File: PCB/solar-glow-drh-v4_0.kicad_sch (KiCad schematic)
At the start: 68 parts, among them J1 UPDI hdr, Q2 DMG1012T, SW2 LED master, U1 AVR64EA28 (VQFN28), U3 ADXL367, U5 NT3H2211, U6 TPS22916C, U7 MB85RC512TY, U8 AEM10300, U9 TPS7A0233PDQNR

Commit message: U6 goes on the board as the DSBGA -- the swap round closes: 0 parity, 0 unconnected, exact ledger, suite 20/20
The board half of the 2026-08-06 ultrathin round, on DRH's rework upload
(merged from main; his Q2 SOT-523 and C9 0603 lands and all wiring kept
verbatim, his sch upload superseded by the branch's -- verified semantically
identical minus the TC1 debug nets).

U6: SC-70 out, solarglow:TPS22916_YFP0004 in at the same centroid, B.Cu,
rot 180 -- chosen so ON's ball sits on R14's x (straight shot north to the
existing junction), VIN diagonals SE to C4.1, VOUT takes one via down and
runs F.Cu east into the old VNFC via's position (that via and its teardrops
retired -- one via total, net fewer than before), GND spokes from the pour.
C6's VS branch rejoins the trunk at its top corner, retiring the dead pad
junction. Ball nets bound A2=VS A1=VNFC B1=GND B2=NFC_EN; fields stamped
from the schematic; silk ref raised to the board's 0.8 floor. NO teardrops
on the balls BY DESIGN -- 0.17 air gap vs the 0.152 floor (README).

TC1: DRH's pad-net choice wins -- sch labels swapped to match his copper
(5=SCL, 6=SDA; 4=BTN stands). His 15 'fix this' exclusions all died with
the swap and the net binding; purged, the 14 ledgered ones kept.

Flow-down: heights U6 1.10->0.50, Q2 1.20->0.90, C9 1.25->0.90 (Diodes
SOT523 A1+A2 max verified from the in-repo sheet); PENDING_FOOTPRINT_SYNC
emptied (all three synced -- stale entries are errors by design); Q2 gets
DIODES_SOT523.step, the missing-stock-model class's third arrival after
U7/U9 (KiCad's SOT-523 footprint names a model kicad-packages3D never
shipped); mask art re-applied (front changed: the VNFC F.Cu run + DRH's
TC1 routing) and MATCHing; coil check OK at C9 47 pF.

Glow window re-measured, teardrop-inclusive, in-aperture: D2 0.3740,
D3 1.2033, D4 1.8112, D5 0.7580 -- bit-identical to the 2026-08-05
baseline. New standing number: INT1-INT2 cross the window at exactly
0.1520 (floor-exact, mid-track, no pads -- not the no-mask-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
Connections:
- net SCL: now also TC1.5, TC1/b1.5; no longer TC1.6, TC1/b1.6
- net SDA: now also TC1.6, TC1/b1.6; no longer TC1.5, TC1/b1.5
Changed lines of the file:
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@@
 		)
 	)
-	(global_label "SDA"
+	(global_label "SCL"
 		(shape bidirectional)
 		(at 405.13 139.7 0)
@@
 		)
 	)
-	(global_label "SCL"
+	(global_label "SDA"
 		(shape bidirectional)
 		(at 405.13 144.78 0)
@@
 		)
 	)
-	(global_label "SDA"
+	(global_label "SCL"
 		(shape bidirectional)
 		(at 405.13 171.45 0)
@@
 		)
 	)
-	(global_label "SCL"
+	(global_label "SDA"
 		(shape bidirectional)
 		(at 405.13 176.53 0)

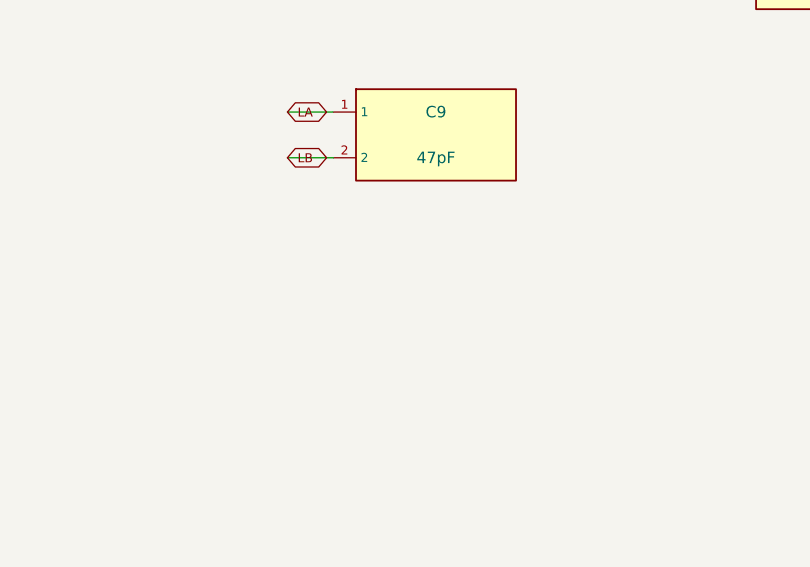
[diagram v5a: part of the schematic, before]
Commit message: C30 -- a DNP trim pad in parallel with C9, the tank's granular-refinement knob
DRH approved the extra pad; here it is, both sides of the parity line.
Schematic: solarglow:C30 (cloned lib symbol), instance at C9's column
wired LA/LB through the same global-label idiom, in_bom no / dnp yes /
in_pos_files no. Board: 0402 at (34.35, 37.95) rot 90, 1.36 mm west of
C9, pads stubbed 0.3 mm-wide to C9's own pads (the tank's track width),
attr smd + exclude_from_pos_files + exclude_from_bom + dnp. NO 3D model
BY CHOICE: the dnp-with-a-model render blind spot (the C9-of-old class)
stays an empty class, and CLAUDE.md's dnp recount moves 12 -> 13 with
the reason.

Why it earns its pads: bench granularity finer than swapping C9
outright, and the AIR variant's retune has a home -- the open 316L
frame drops the ferrite, L falls toward the bare 0.958 uH, f0 rises,
and the correction is MORE parallel C: exactly the direction a parallel
pad adds. (C9's own history ran the other way: the 82 pF + DNP
arrangement of the pre-2026-07-30 tune sat UNDER the carrier. This pad
cannot repeat that mistake -- C9's 47 pF keeps the enclosed tank above
13.56 on its own, and C30 only ever pulls DOWN toward it.)

Verified: ERC 3 pre-existing excluded warnings only (grid-snapped after
the first pass caught my off-grid 15.62 offset -- 16.51 is 13 steps);
parity DRC NO unexcluded errors, 0 unconnected (one courtyard kiss
found and fixed by the 0.25 westward shift); mask_art MATCH;
consistency 0/0. Buy documents untouched by construction: dnp keeps C30
out of the BOM, the CPL, and check [15]'s ledger until a value exists.

Co-Authored-By: Claude Fable 5 <noreply@anthropic.com>
Claude-Session: https://claude.ai/code/session_015D4iTho3BuNxSQyJmyaxvg
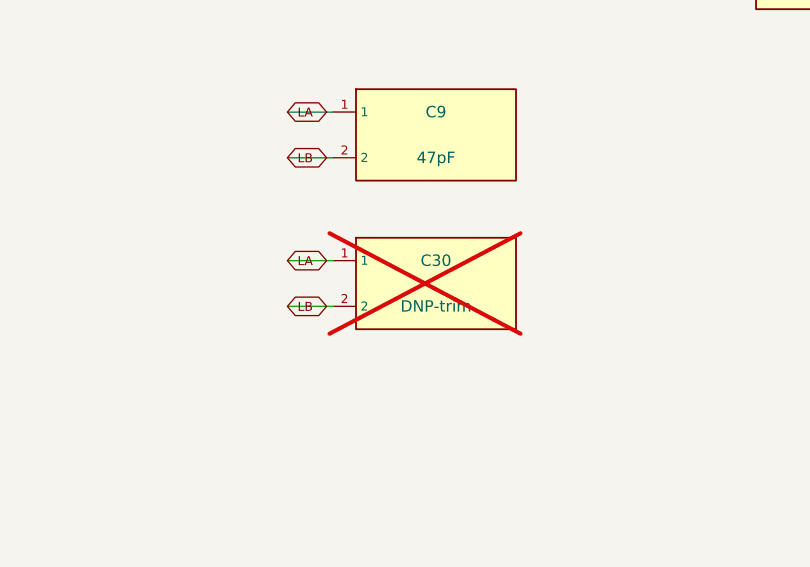
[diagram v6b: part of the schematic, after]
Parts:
- added C30: DNP-trim, Capacitor_SMD:C_0402_1005Metric, symbol solarglow:C30
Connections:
- net LA: now also C30.1
- net LB: now also C30.2
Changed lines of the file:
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@@
 	)
 	(symbol
+		(lib_id "solarglow:C30")
+		(at 560.07 135.89 0)
+		(unit 1)
+		(body_style 1)
+		(exclude_from_sim no)
+		(in_bom no)
+		(on_board yes)
+		(in_pos_files no)
+		(dnp yes)
+		(property "Reference" "C30"
+			(at 571.5 135.89 0)
+			(show_name no)
+			(do_not_autoplace no)
+			(effects
+				(font
+					(size 1.27 1.27)
+				)
+			)
+		)
+		(property "Value" "DNP-trim"
+			(at 571.5 140.97 0)
+			(show_name no)
+			(do_not_autoplace no)
+			(effects
+				(font
+					(size 1.27 1.27)
+				)
+			)
+		)
+		(property "Footprint" "Capacitor_SMD:C_0402_1005Metric"
+			(at 571.5 129.54 0)
+			(hide yes)
+			(show_name no)
+			(do_not_autoplace no)
+			(effects
+				(font
+					(size 1.27 1.27)
+				)
+			)
+		)
+		(property "Datasheet" ""
+			(at 560.07 135.89 0)
+			(hide yes)
+			(show_name no)
+			(do_not_autoplace no)
+			(effects
+				(font
+					(size 1.27 1.27)
+				)
+			)
+		)
+		(property "Description" "C9 tank trim pad, DNP (2026-08-07). Parallel with C9 across LA/LB: bench granularity for the paper-tune ladder, and headroom for the AIR variant retune -- the open 316L frame drops the ferrite, L falls toward the bare 0.958 uH, f0 rises, and the fix is MORE C in parallel: exactly what this pad adds. Fit a High-Q C0G 0402 chosen at the bench; stays out of every buy document until a value exists (dnp + exclude_from_bom + exclude_from_pos_files)."
+			(at 560.07 135.89 0)
+			(hide yes)
+			(show_name no)
+			(do_not_autoplace no)
+			(effects
+				(font
+					(size 1.27 1.27)
+				)
+			)
+		)
+		(property "MPN" "QSCP251Q470G1GV001T"
+			(at 560.07 135.89 0)
+			(hide yes)
+			(show_name no)
+			(do_not_autoplace no)
+			(effects
+				(font
+					(size 1.27 1.27)
+				)
+			)
+		)
+		(property "Manufacturer" "Johanson Technology"
+			(at 560.07 135.89 0)
+			(hide yes)
+			(show_name no)
+			(do_not_autoplace no)
+			(effects
+				(font
+					(size 1.27 1.27)
+				)
+			)
+		)
+		(property "Supplier" "DigiKey"
+			(at 560.07 135.89 0)
+			(hide yes)
+			(show_name no)
+			(do_not_autoplace no)
+			(effects
+				(font
+					(size 1.27 1.27)
+				)
+			)
+		)
+		(property "Supplier P/N" "712-QSCP251Q470G1GV001TCT-ND"
+			(at 560.07 135.89 0)
+			(hide yes)
+			(show_name no)
+			(do_not_autoplace no)
+			(effects
+				(font
+					(size 1.27 1.27)
+				)
+			)
+		)
+		(pin "1"
+		)
+		(pin "2"
+		)
+		(instances
+			(project "solar-glow-drh-v4_0"
+				(path "/bf17630f-b49b-49a7-9335-83fa0a7a44d0"
+					(reference "C30")
+					(unit 1)
+				)
+			)
+		)
+	)
+	(symbol
 		(lib_id "solarglow:SC1")
 		(at 80.01 38.1 0)
@@
 		)
 	)
+	(global_label "LA"
+		(shape bidirectional)
+		(at 554.99 135.89 0)
+		(effects
+			(font
+				(size 1 1)
+			)
+		)
+		(property "Intersheetrefs" "${INTERSHEET_REFS}"
+			(at 554.99 135.89 0)
+			(hide yes)
+			(show_name no)
+			(do_not_autoplace no)
+			(effects
+				(font
+					(size 1.27 1.27)
+				)
+			)
+		)
+	)
+	(global_label "LB"
+		(shape bidirectional)
+		(at 554.99 140.97 0)
+		(effects
+			(font
+				(size 1 1)
+			)
+		)
+		(property "Intersheetrefs" "${INTERSHEET_REFS}"
+			(at 554.99 140.97 0)
+			(hide yes)
+			(show_name no)
+			(do_not_autoplace no)
+			(effects
+				(font
+					(size 1.27 1.27)
+				)
+			)
+		)
+	)
+	(wire
+		(pts
+			(xy 560.07 135.89) (xy 554.99 135.89)
+		)
+		(stroke
+			(width 0)
+			(type default)
+		)
+	)
+	(wire
+		(pts
+			(xy 560.07 140.97) (xy 554.99 140.97)
+		)
+		(stroke
+			(width 0)
+			(type default)
+		)
+	)

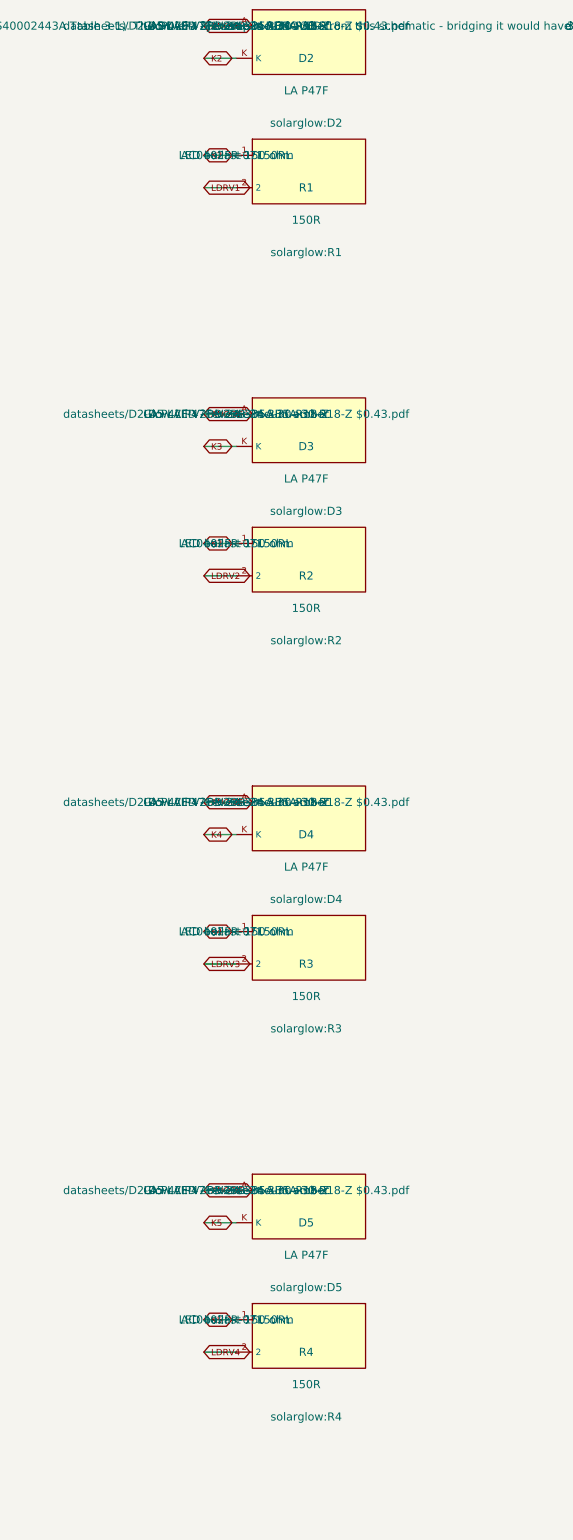
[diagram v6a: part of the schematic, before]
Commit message: RN1 -- DRH's 4-in-1 ballast array, identified, verified, and flowed through the whole repo
DRH drew the copper (KiCad R_Array_Convex_4x0402 land, mid-board at
(32.03, 49.84), R1-R4 deleted); this finishes everything downstream.

THE PART, from a 12-agent verified sourcing sweep (3 finders, 8
adversarial verifies, 1 judge; every claim pulled from the live catalog
or DigiKey page): Panasonic EXB-28V151JX, 4x150R isolated, 0804 convex.
The +/-1% grades all failed procurement reality (Yageo YC124-FR is
marketplace-only at 10k MOQ/17wk; KOA CN1E4 family-EOL; CTS unlisted),
making J +/-5% the buyable ceiling -- the tie broke on AEC-Q200 Grade 1
in the CURRENT catalog (Yageo WITHDREW their claim in DS V.11 Sep 2025;
DigiKey's attribute is stale against it), 0.45 max height (0.15 under
the lite brace's 0.60 span), 136,179 live DigiKey stock, and the
strongest pairing evidence in the pool: the catalog PRINTS the pin
numbers -- elements 1-8/2-7/3-6/4-5, IC-style -- matching the board's
wiring exactly. A different convention would PERMUTE the LED channels;
that check was load-bearing, not paranoia. Sourcing record lives in
RN1's own Description field. Runner-up: YC124-JR-07150RL.

Schematic: R1-R4 excised whole (instances, lib defs, wires, labels);
solarglow:RN1 8-pin symbol wired through the same global-label idiom,
pin-for-pin to the board (parity proves it: 0 unconnected, 0 field
mismatches). Board: footprint annotated RN1, linked to the schematic
uuid, MPN/Manufacturer/Supplier P/N mirrored. The stock land's own
0.150 inter-pad gap (2um under the 0.152 floor) fixed BY DESIGN: inner
pads slimmed 0.300 -> 0.294 -> gap 0.153, no exclusions carried;
PCB/README's re-link warning box records it so Update-Footprints-from-
Library cannot silently revert it.

Flow-down: part_heights RN1 0.45 (catalog T max); check [20]'s
OPAQUE_PN_LEDGER gains ("EXB-28V151JX","Y7151CT-ND") and drops the
orphaned R1-R4 Yageo pair per its own instruction (with a syntax
mishap en route: a naive insert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
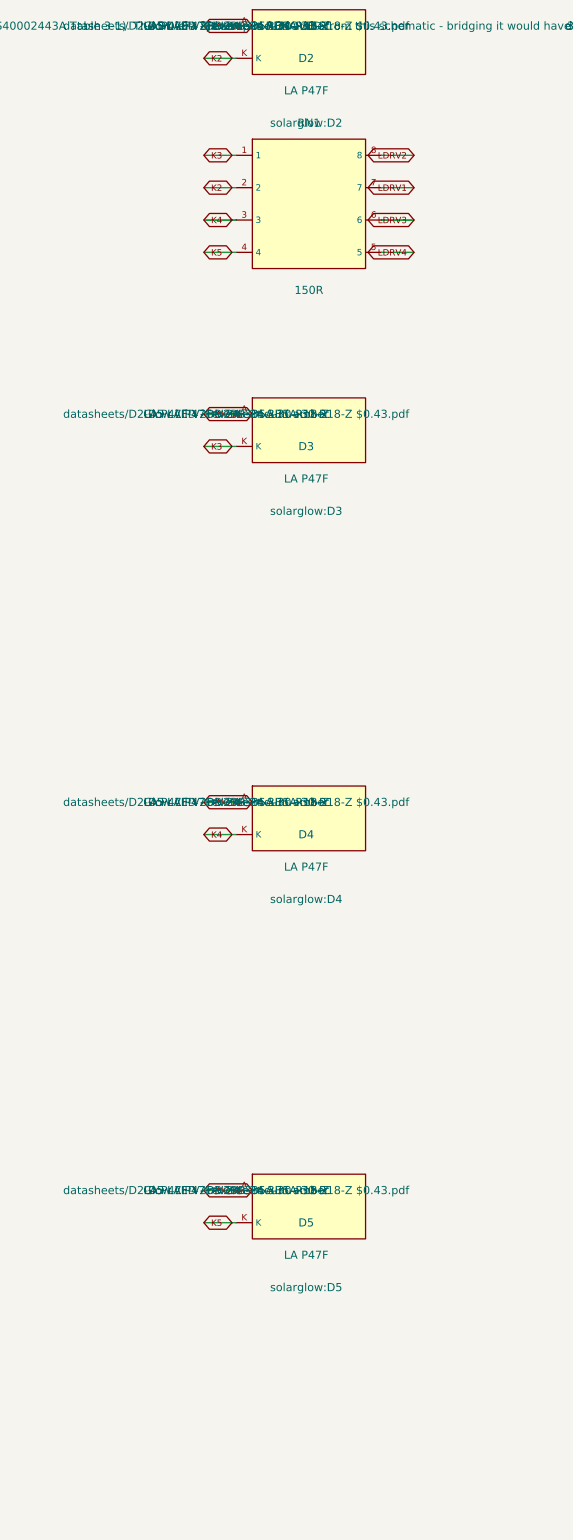
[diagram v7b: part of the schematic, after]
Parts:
- removed R1: 150R, solarglow:R1, symbol solarglow:R1
- removed R2: 150R, solarglow:R2, symbol solarglow:R2
- removed R3: 150R, solarglow:R3, symbol solarglow:R3
- removed R4: 150R, solarglow:R4, symbol solarglow:R4
- added RN1: 150R, Resistor_SMD:R_Array_Convex_4x0402, symbol solarglow:RN1
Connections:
- net K2: now also RN1.2
- net K3: now also RN1.1
- net K4: now also RN1.3
- net K5: now also RN1.4
- net LDRV1: now also RN1.7
- net LDRV2: now also RN1.8
- net LDRV3: now also RN1.6
- net LDRV4: now also RN1.5

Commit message: RN2 + the 2M bump + the decoupling census -- three fewer parts, one repaired schematic
The consolidation round DRH asked for, plus what it uncovered:

- RN2 (Panasonic EXB-24V472JX, 2x4.7k convex array) replaces R10/R11 at
  (28.4, 32.95) B-side, pads rotated 270 (a pad's stored angle is TOTAL
  rotation -- an angle-less pad sits axis-aligned and shaved the SDA-trunk
  gap to 0.124; ledgered in PCB/README). Board pin order is VS/VS/SCL/SDA;
  the schematic labels match it. Elements pair 1-4/2-3, both signal->VS.
  Dead R10-feed chain (3 segments) and a C7-era elbow pruned; DRC 0 errors,
  0 unconnected, 0 parity.

- R5/R6 VSENSE divider 1M -> 2M: Vishay MCT0603MD2004BP500, the only 0603
  holding +/-25 ppm/K guaranteed at 2M (Yageo's 2M is 50 ppm and stockless).
  Halves the divider's permanent SRC bleed, and the MPN merges with R15's
  existing line -- one distinct part fewer to buy.

- The 100nF census (9 after the round, each with a named pin): C7 deleted --
  it double-decoupled U6.A2 beside C6, a leftover from U6's SC-70 era.
  C1/C29 are NOT redundant (U1 has two VS pins). Standing flag: C8 sits
  5.25 mm from U5.6 VNFC -- relocation queued for DRH's next copper session.

- Schematic repair: RN1's instance block carried C9's full sourcing tail
  (Johanson MPN/Manufacturer/Supplier/712- P/N) from the PR #213 clone --
  parity read RN1's MPN as the 47pF cap's, and the stray Supplier field was
  what made check [20] classify Y7151CT-ND correctly, by accident. Tail
  removed from RN1 (and RN2's inherited copy); C30's wrong-case QSCP
  sourcing fields stripped (bench-pick part, DNP, no MPN by design);
  Supplier "DigiKey" restored as a real field on both arrays and mirrored
  to their footprints.

- Gates: ledger [20] RN2 pair in, R10/R11 orphan out; part_heights RN2 0.45;
  check_mesh re-ledgered both braces (RN2 pocket in, R10/R11/C7 pockets
  out); interference_drc green on max+lite against the regenerated braces.
  The 2x0402 STEP model lands pre-coloured from 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
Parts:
- removed C7: 100nF, solarglow:C7, symbol solarglow:C7
- removed R10: 4.7k, solarglow:R10, symbol solarglow:R10
- removed R11: 4.7k, solarglow:R11, symbol solarglow:R11
- added RN2: 4.7k, Resistor_SMD:R_Array_Convex_2x0402, symbol solarglow:RN2
- C30: MPN QSCP251Q470G1GV001T -> (none); Manufacturer Johanson Technology -> (none); Supplier DigiKey -> (none); Supplier P/N 712-QSCP251Q470G1GV001TCT-ND -> (none)
- R5, R6: value 1M -> 2M; MPN RT0603BRD071ML -> MCT0603MD2004BP500; Manufacturer Yageo -> Vishay; Supplier P/N YAG4498CT-ND -> 541-MCT0603MD2004BP500CT-ND
- RN1: MPN QSCP251Q470G1GV001T -> EXB-28V151JX; Manufacturer Johanson Technology -> Panasonic; Supplier P/N 712-QSCP251Q470G1GV001TCT-ND -> Y7151CT-ND
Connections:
- net SCL: now also RN2.3
- net SDA: now also RN2.4
- net VS: now also RN2.1, RN2.2
